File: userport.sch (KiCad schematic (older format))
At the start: 24 parts, among them CN10 USERPORT, U122 74LS654, U21 74HCT04, U22 MOS_6529, U23 MOS_6551_ACIA, U28 GAL16V8, Y2 1.8432M

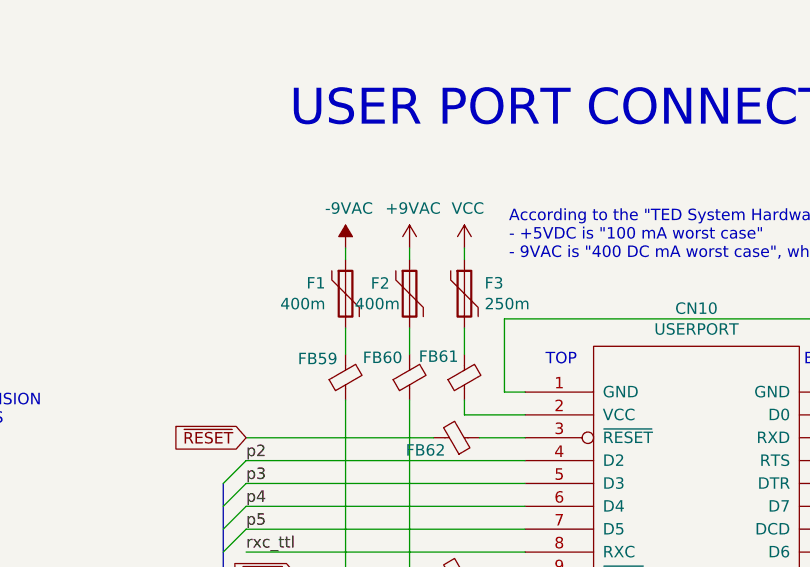
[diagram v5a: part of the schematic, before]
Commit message: Use resettable fuses everywhere we do current limiting
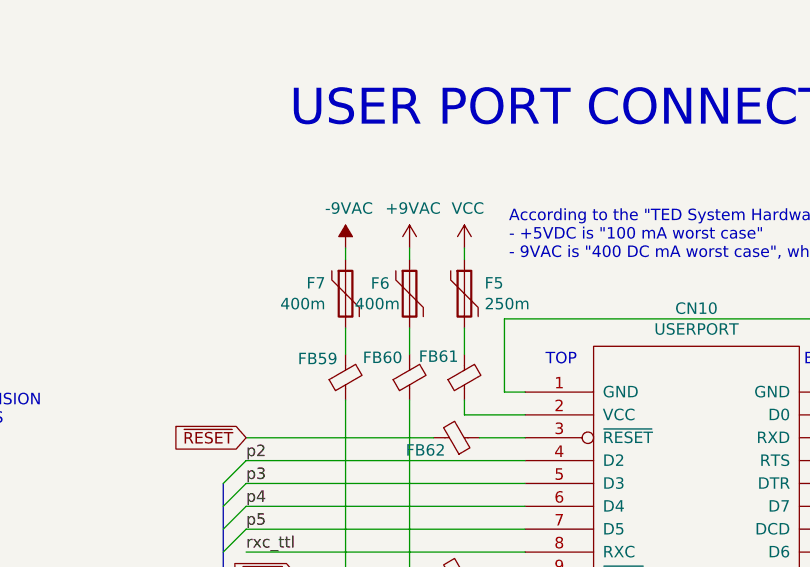
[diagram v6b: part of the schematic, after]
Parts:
- F5: renamed from F3; footprint Fuse:Fuse_Bourns_MF-RG400 -> LittleSixteen:Fuse_Bourns
- F6: renamed from F2; footprint Fuse:Fuse_Bourns_MF-RG400 -> LittleSixteen:Fuse_Bourns
- F7: renamed from F1; footprint Fuse:Fuse_Bourns_MF-RG400 -> LittleSixteen:Fuse_Bourns
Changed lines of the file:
@@
 	13500 1520 13950 1520
 $Comp
-L Device:Polyfuse F3
+L Device:Polyfuse F5
 U 1 1 677AFD86
 P 7425 6100
-F 0 "F3" H 7513 6146 50  0000 L CNN
+F 0 "F5" H 7513 6146 50  0000 L CNN
 F 1 "250m" H 7513 6055 50  0000 L CNN
-F 2 "Fuse:Fuse_Bourns_MF-RG400" H 7475 5900 50  0001 L CNN
+F 2 "LittleSixteen:Fuse_Bourns" H 7475 5900 50  0001 L CNN
 F 3 "~" H 7425 6100 50  0001 C CNN
 F 4 "603-BK60-025-DZ" H 7425 6100 50  0001 C CNN "MouserPN"
@@
 $EndComp
 $Comp
-L Device:Polyfuse F1
+L Device:Polyfuse F7
 U 1 1 677B0E80
 P 6905 6100
-F 0 "F1" H 6817 6146 50  0000 R CNN
+F 0 "F7" H 6817 6146 50  0000 R CNN
 F 1 "400m" H 6817 6055 50  0000 R CNN
-F 2 "Fuse:Fuse_Bourns_MF-RG400" H 6955 5900 50  0001 L CNN
+F 2 "LittleSixteen:Fuse_Bourns" H 6955 5900 50  0001 L CNN
 F 3 "~" H 6905 6100 50  0001 C CNN
 F 4 "603-BK60-040-DI" H 6905 6100 50  0001 C CNN "MouserPN"
@@
 $EndComp
 $Comp
-L Device:Polyfuse F2
+L Device:Polyfuse F6
 U 1 1 677B15C8
 P 7185 6100
-F 0 "F2" H 7015 6145 50  0000 L CNN
+F 0 "F6" H 7015 6145 50  0000 L CNN
 F 1 "400m" H 6945 6055 50  0000 L CNN
-F 2 "Fuse:Fuse_Bourns_MF-RG400" H 7235 5900 50  0001 L CNN
+F 2 "LittleSixteen:Fuse_Bourns" H 7235 5900 50  0001 L CNN
 F 3 "~" H 7185 6100 50  0001 C CNN
 F 4 "603-BK60-040-DI" H 7185 6100 50  0001 C CNN "MouserPN"

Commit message: Minor fixes + P/N updates
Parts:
- U21: MouserPN (none) -> 595-SN74HCT04N
- Y2: MouserPN (none) -> 520-HCA184-SX
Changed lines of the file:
@@
 F 3 "~" H 2685 2705 50  0001 C CNN
 F 4 "Series, no load cap, max series resistance: 400R" H 2685 2705 50  0001 C CNN "Notes"
+F 5 "520-HCA184-SX" H 2685 2705 50  0001 C CNN "MouserPN"
 	1    2685 2705
 	0    -1   -1   0
@@
 F 2 "LittleSixteen:DIP-14_W7.62mm_Socket_LongPads" H 8690 2745 50  0001 C CNN
 F 3 "http://www.ti.com/lit/gpn/sn74LS04" H 8690 2745 50  0001 C CNN
+F 4 "595-SN74HCT04N" H 8690 2745 50  0001 C CNN "MouserPN"
 	1    8690 2745
 	1    0    0    -1
@@
 F 2 "LittleSixteen:DIP-14_W7.62mm_Socket_LongPads" H 8690 2340 50  0001 C CNN
 F 3 "http://www.ti.com/lit/gpn/sn74LS04" H 8690 2340 50  0001 C CNN
+F 4 "595-SN74HCT04N" H 8690 2340 50  0001 C CNN "MouserPN"
 	2    8690 2340
 	1    0    0    -1
@@
 F 2 "LittleSixteen:DIP-14_W7.62mm_Socket_LongPads" H 8690 3210 50  0001 C CNN
 F 3 "http://www.ti.com/lit/gpn/sn74LS04" H 8690 3210 50  0001 C CNN
+F 4 "595-SN74HCT04N" H 8690 3210 50  0001 C CNN "MouserPN"
 	3    8690 3210
 	-1   0    0    -1
@@
 F 2 "LittleSixteen:DIP-14_W7.62mm_Socket_LongPads" H 8690 3655 50  0001 C CNN
 F 3 "http://www.ti.com/lit/gpn/sn74LS04" H 8690 3655 50  0001 C CNN
+F 4 "595-SN74HCT04N" H 8690 3655 50  0001 C CNN "MouserPN"
 	4    8690 3655
 	-1   0    0    -1
@@
 F 2 "LittleSixteen:DIP-14_W7.62mm_Socket_LongPads" H 11070 10770 50  0001 C CNN
 F 3 "http://www.ti.com/lit/gpn/sn74LS04" H 11070 10770 50  0001 C CNN
+F 4 "595-SN74HCT04N" H 11070 10770 50  0001 C CNN "MouserPN"
 	5    11070 10770
 	1    0    0    -1
@@
 F 2 "LittleSixteen:DIP-14_W7.62mm_Socket_LongPads" H 2975 10020 50  0001 C CNN
 F 3 "http://www.ti.com/lit/gpn/sn74LS04" H 2975 10020 50  0001 C CNN
+F 4 "595-SN74HCT04N" H 2975 10020 50  0001 C CNN "MouserPN"
 	7    2975 10020
 	1    0    0    -1
